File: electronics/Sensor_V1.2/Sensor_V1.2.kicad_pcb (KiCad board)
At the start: 2 copper layers, 45.9 x 25.6 mm, 44 parts, among them J1 nuclone_small_left, J2 nuclone_small_right, J5 DevBoardUartInput, Q1 DMG1012, Q2 DMG1012, Q3 DMG1012, U1 PPG_sensor, U2 reference_sot23-3, U3 MCP6541

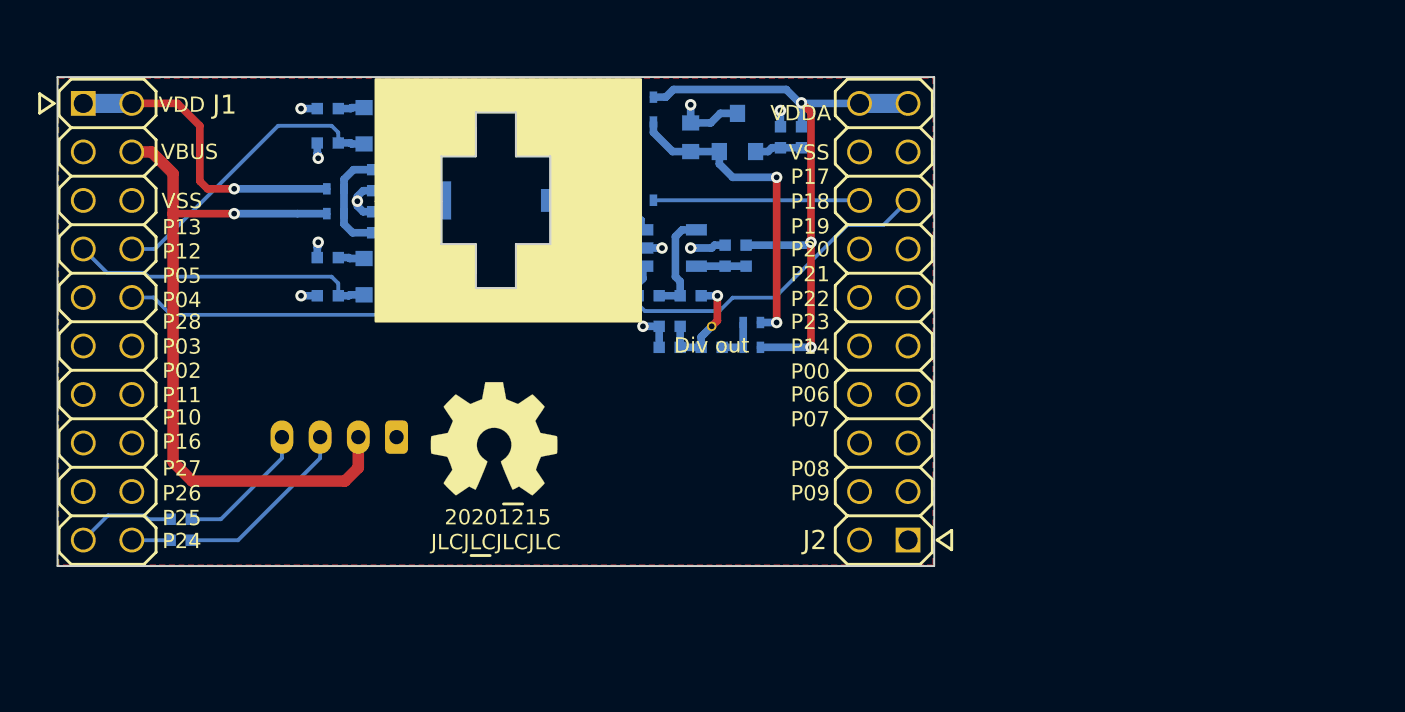
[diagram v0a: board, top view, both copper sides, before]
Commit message: imported some changed components, but need to redo the footprints from TODO
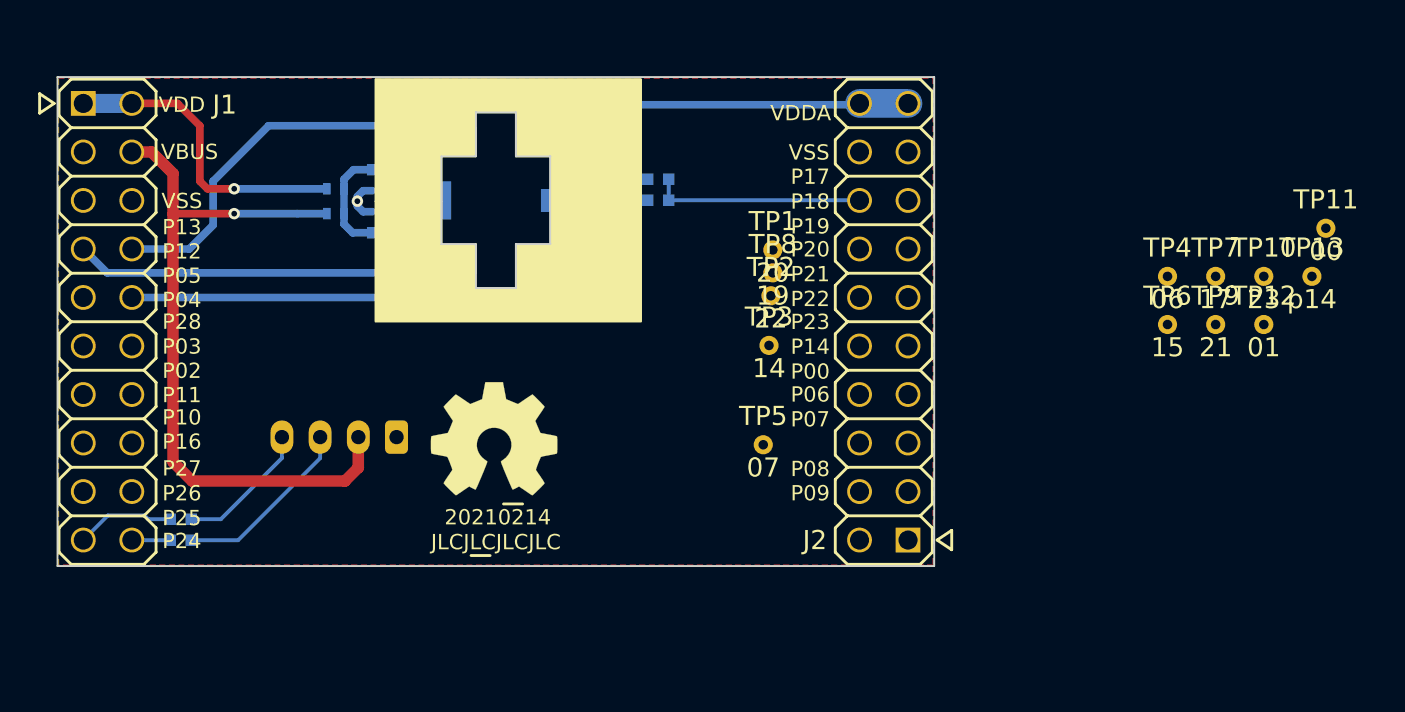
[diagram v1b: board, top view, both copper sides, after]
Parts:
- removed C10, C11, C5: 1u, SquantorRcl:C_0402
- removed C3: 100n, SquantorRcl:C_0402
- removed C6: 10u, SquantorRcl:C_0603
- removed FB1, FB2: Ferrite_Bead, SquantorRcl:L_0402
- removed JP1: bias VDD, SquantorSpecial:solder_jumper_2way_noconn
- removed JP3: bias REF, SquantorSpecial:solder_jumper_2way_noconn
- removed JP4: AVDD divider, SquantorSpecial:solder_jumper_2way_noconn
- removed JP5: VREF divider, SquantorSpecial:solder_jumper_2way_noconn
- removed JP7: PD_ADC, SquantorSpecial:solder_jumper_2way_noconn
- removed Q2, Q3: DMG1012, SquantorIC:SOT23-3
- removed R12, R17, R18, R7: R, SquantorRcl:R_0402_hand
- removed R5, R6: 10K, SquantorRcl:R_0402_hand
- removed U2: reference_sot23-3, SquantorIC:SOT23-3
- removed U3: MCP6541, SquantorIC:SOT23-5-Microchip-OT
- added TP1: 20, SquantorTestPoints:TestPoint_hole_H05R10, F.Cu at (99.6, 82.6)
- added TP10: 23, SquantorTestPoints:TestPoint_hole_H05R10, F.Cu at (125.3, 84.0)
- added TP12: 01, SquantorTestPoints:TestPoint_hole_H05R10, F.Cu at (125.3, 86.5)
- added TP13: p14, SquantorTestPoints:TestPoint_hole_H05R10, F.Cu at (127.8, 84.0)
- added TP2: 22, SquantorTestPoints:TestPoint_hole_H05R10, F.Cu at (99.5, 85.0)
- added TP3: 14, SquantorTestPoints:TestPoint_hole_H05R10, F.Cu at (99.4, 87.6)
- added TP4: 06, SquantorTestPoints:TestPoint_hole_H05R10, F.Cu at (120.3, 84.0)
- added TP5: 07, SquantorTestPoints:TestPoint_hole_H05R10, F.Cu at (99.1, 92.8)
- added TP6: 15, SquantorTestPoints:TestPoint_hole_H05R10, F.Cu at (120.3, 86.5)
- added TP7: 17, SquantorTestPoints:TestPoint_hole_H05R10, F.Cu at (122.8, 84.0)
- added TP8: 19, SquantorTestPoints:TestPoint_hole_H05R10, F.Cu at (99.6, 83.8)
- added TP9: 21, SquantorTestPoints:TestPoint_hole_H05R10, F.Cu at (122.8, 86.5)
- C2: value 100n -> TBD
- N2: value 20201215 -> 20210214
- R3, R4: value 100 -> TBD
- TP11: value Div out -> 00; footprint SquantorTestPoints:TestPoint_hole_H03R05 -> SquantorTestPoints:TestPoint_hole_H05R10
- moved TP11 32.6 mm to (128.6, 81.5)
- moved R4 18.0 mm to (93.6, 80.0)
- moved R3 15.7 mm to (91.6, 79.4), turned to 90 degrees
- moved C2 14.5 mm to (93.6, 78.9), turned to 0 degrees
- moved C1 1.40 mm to (90.2, 76.1)
- moved FB3 0.80 mm to (90.2, 75.0)
- moved R8 0.30 mm to (89.7, 85.0)
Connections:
- C2 pad 1: /LED1_A -> /VSS
- C2 pad 2: /VSS -> /PD_ADC
- FB3 pad 1: Net-(FB3-Pad1) -> /VDDA
- J1 pad 7: /LED1_EN -> /LED1_C
- J1 pad 8: /LED2_EN -> /LED2_C
- J2 pad 1: Net-(J2-Pad1) -> /GPIO_14
- J2 pad 10: Net-(J2-Pad10) -> /P0_14
- J2 pad 11: Net-(J2-Pad11) -> /P0_21
- J2 pad 12: Net-(J2-Pad12) -> /P0_22
- J2 pad 13: Net-(J2-Pad13) -> /P0_19
- J2 pad 14: Net-(J2-Pad14) -> /P0_20
- J2 pad 15: /CMP_OUT -> /P0_17
- J2 pad 2: Net-(J2-Pad2) -> /P0_15
- J2 pad 3: Net-(J2-Pad3) -> /P0_01
- J2 pad 6: Net-(J2-Pad6) -> /P0_07
- J2 pad 7: Net-(J2-Pad7) -> /P0_00
- J2 pad 8: Net-(J2-Pad8) -> /P0_06
- J2 pad 9: Net-(J2-Pad9) -> /P0_23
- R3 pad 1: Net-(Q2-Pad2) -> /PD_OUT
- R4 pad 1: Net-(Q3-Pad2) -> /PD_ADC
- R4 pad 2: /VSS -> /PD_OUT
- TP11 pad 1: /Divider_out -> /P0_00
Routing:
- net /CMP_OUT: track 18.8 -> 0.00 mm
- net /VDDA: track 34.4 -> 16.0 mm, vias 3 -> 0
- net /LED2_C: track 9.06 -> 27.2 mm
- net /LED1_C: track 9.06 -> 26.4 mm
- net /VREF: track 16.8 -> 0.00 mm, vias 2 -> 0
- net /LED1_EN: track 16.1 -> 0.00 mm
- net /LED2_EN: track 15.5 -> 0.00 mm
- net /VSS: track 20.3 -> 9.31 mm, vias 13 -> 5
- net /Divider_out: track 6.10 -> 0.00 mm, vias 1 -> 0
- net Net-(R17-Pad2): track 5.55 -> 0.00 mm
- net Net-(FB3-Pad1): track 3.04 -> 0.00 mm
- net Net-(C10-Pad1): track 2.60 -> 0.00 mm
- net Net-(C5-Pad1): track 2.48 -> 0.00 mm
- net Net-(JP4-Pad2): track 2.40 -> 0.00 mm
- net /PD_BIAS: track 15.9 -> 14.0 mm, vias 2 -> 1
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
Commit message: initial placement of components
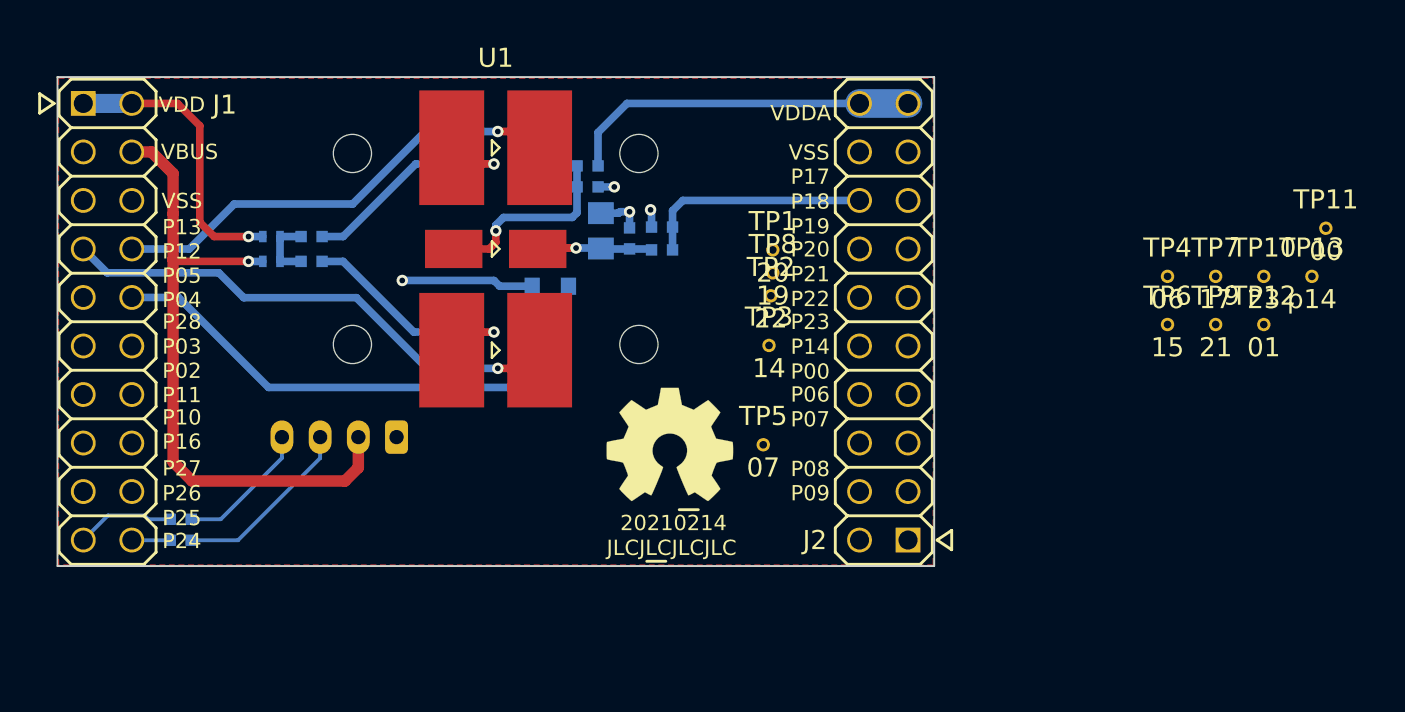
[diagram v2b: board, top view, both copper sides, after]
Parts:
- TP1, TP10, TP11, TP12, TP13, TP2, TP3, TP4, TP5, TP6, TP7, TP8, TP9: footprint SquantorTestPoints:TestPoint_hole_H05R10 -> SquantorTestPoints:TestPoint_hole_H04R07
- U1: footprint SquantorOpto:PPG_sensor_reverse_PD_antiparallel -> SquantorOpto:PPG_sensor_front_universal
- moved N1 9.20 mm to (94.2, 92.8)
- moved N2 9.20 mm to (95.2, 96.8)
- moved N3 9.20 mm to (93.5, 98.3)
- moved R11 5.13 mm to (75.5, 81.9)
- moved JP2 4.18 mm to (73.3, 81.9)
- moved JP6 4.18 mm to (73.3, 83.2)
- moved R10 4.04 mm to (75.5, 83.2)
- moved C1 3.21 mm to (89.9, 79.3)
- moved FB3 3.21 mm to (89.9, 78.2)
- moved C9 2.65 mm to (90.6, 81.6)
- moved R3 2.65 mm to (92.1, 82.0)
- moved R4 2.61 mm to (93.8, 82.6)
- moved U1 2.54 mm to (85.1, 82.5)
- moved C2 2.51 mm to (93.8, 81.4)
- moved R8 2.33 mm to (87.5, 85.9)
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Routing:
- net /LED1_A: track 5.24 -> 13.1 mm, vias 0 -> 1
- net /LED2_A: track 5.28 -> 13.1 mm, vias 0 -> 1
- net /PD_BIAS: track 14.0 -> 10.2 mm
- net /VBUS: track 37.8 -> 34.5 mm
- net /VSS: track 9.31 -> 12.5 mm, vias 5 -> 4
- net /LED2_C: track 27.2 -> 24.2 mm, vias 0 -> 1
- net /VDDA: track 16.0 -> 18.6 mm
- net /LED_VDD: track 5.74 -> 3.50 mm
- net /VDD: track 16.3 -> 15.2 mm
- net /PD_ADC: track 11.1 -> 12.1 mm
- net /I_reset: track 28.4 -> 29.3 mm
- net /PD_OUT: track 6.46 -> 7.37 mm, vias 0 -> 1
- net /LED1_C: track 26.4 -> 26.9 mm, vias 0 -> 1
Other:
- outline, holes or cut-outs redrawn

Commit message: components placed, changing silk
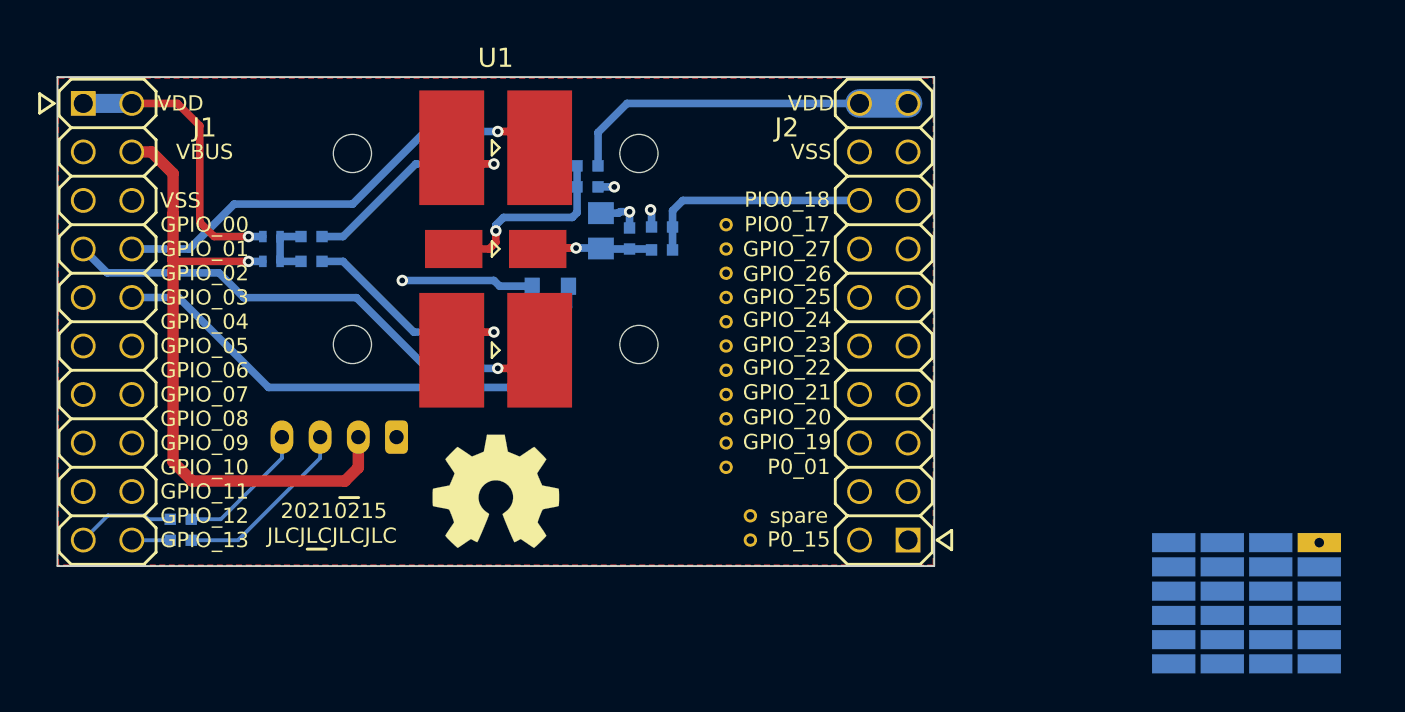
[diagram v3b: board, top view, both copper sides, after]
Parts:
- added J3: Proto_1pin, SquantorProto:proto-SMD-0127-08X06-P010X020+pin, B.Cu at (124.4, 101.1)
- J1: footprint SquantorConnectors:Header-0254-2X10-H010 -> SquantorConnectorsNamed:nuclone_small_left
- J2: footprint SquantorConnectors:Header-0254-2X10-H010 -> SquantorConnectorsNamed:nuclone_small_right
- N2: value 20210214 -> 20210215
- TP1, TP10, TP11, TP12, TP13, TP2, TP3, TP4, TP5, TP6, TP7, TP8, TP9: moved to B.Cu
- moved TP11 32.9 mm to (97.2, 91.4)
- moved TP13 32.0 mm to (98.4, 96.5)
- moved TP12 29.1 mm to (97.2, 94.0)
- moved TP10 28.6 mm to (97.2, 88.9)
- moved TP7 25.8 mm to (97.2, 81.3)
- moved TP9 25.6 mm to (97.2, 86.4)
- moved TP6 24.6 mm to (98.4, 97.8)
- moved TP4 23.9 mm to (97.2, 90.2)
- moved N2 17.8 mm to (77.4, 96.2)
- moved N3 17.8 mm to (75.7, 97.7)
- moved N1 9.43 mm to (85.1, 95.2)
- moved TP1 2.45 mm to (97.2, 82.5)
- moved TP8 2.45 mm to (97.2, 83.8)
- moved TP2 2.35 mm to (97.2, 85.1)
- moved TP3 2.25 mm to (97.2, 87.6)
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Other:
- board text removed: "P00"
- board text removed: "P02"
- board text removed: "P03"
- board text removed: "P04"
- board text removed: "P05"
- board text removed: "P06"
- board text removed: "P07"
- board text removed: "P08"
- board text removed: "P09"
- board text removed: "P10"
- board text removed: "P11"
- board text removed: "P12"
- board text removed: "P13"
- board text removed: "P14"
- board text removed: "P16"
- board text removed: "P17"
- board text removed: "P18"
- board text removed: "P19"
- board text removed: "P20"
- board text removed: "P21"
- board text removed: "P22"
- board text removed: "P23"
- board text removed: "P24"
- board text removed: "P25"
- board text removed: "P26"
- board text removed: "P27"
- board text removed: "P28"
- board text removed: "VBUS"
- board text removed: "VDD"
- board text removed: "VDDA"
- board text removed: "VSS"

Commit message: changed header labels, changed test point labels
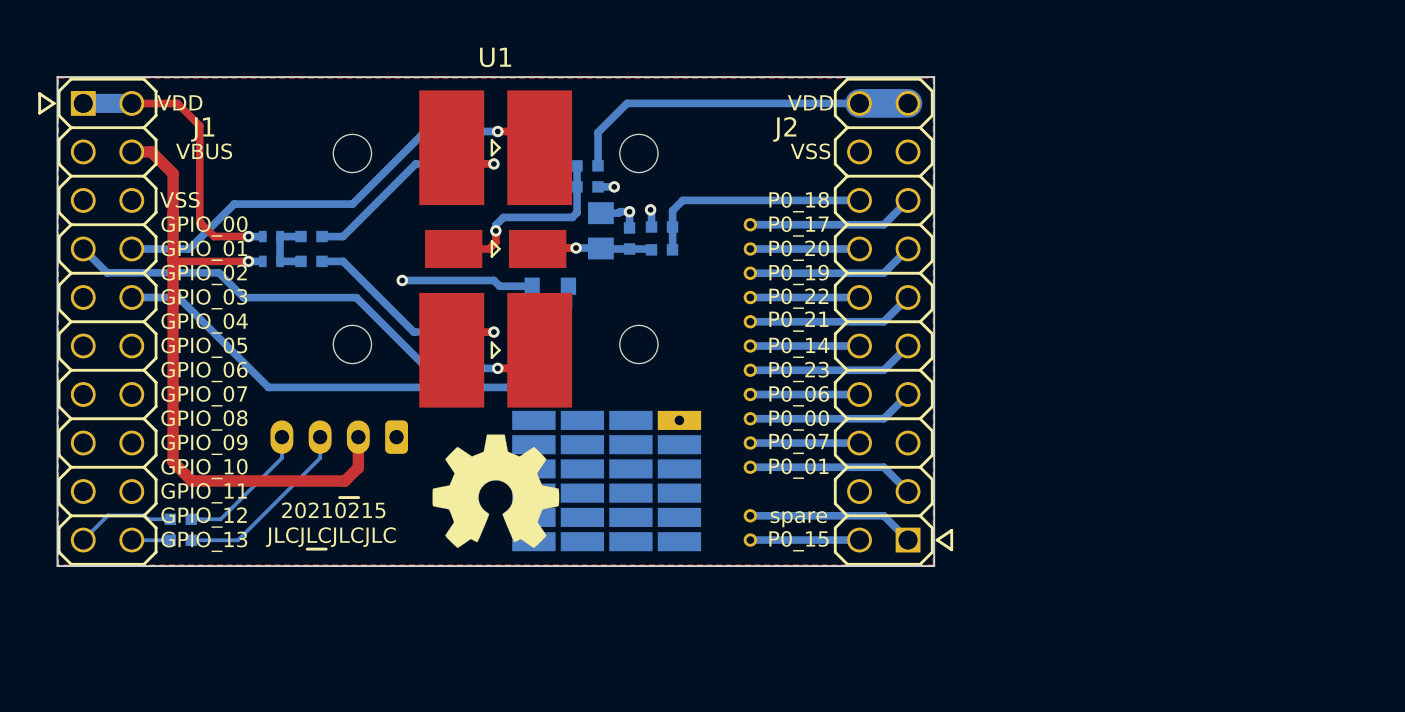
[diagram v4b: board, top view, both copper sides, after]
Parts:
- moved J3 34.1 mm to (90.9, 94.7)
- moved TP1 1.27 mm to (98.4, 82.5)
- moved TP10 1.27 mm to (98.4, 88.9)
- moved TP11 1.27 mm to (98.4, 91.4)
- moved TP12 1.27 mm to (98.4, 94.0)
- moved TP2 1.27 mm to (98.4, 85.1)
- moved TP3 1.27 mm to (98.4, 87.6)
- moved TP4 1.27 mm to (98.4, 90.2)
- moved TP5 1.27 mm to (98.4, 92.7)
- moved TP7 1.27 mm to (98.4, 81.3)
- moved TP8 1.27 mm to (98.4, 83.8)
- moved TP9 1.27 mm to (98.4, 86.4)
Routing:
- net /P0_23: track 0.00 -> 8.78 mm
- net /GPIO_14: track 0.00 -> 8.78 mm
- net /P0_21: track 0.00 -> 8.78 mm
- net /P0_19: track 0.00 -> 8.78 mm
- net /P0_17: track 0.00 -> 8.78 mm
- net /P0_01: track 0.00 -> 8.78 mm
- net /P0_00: track 0.00 -> 8.78 mm
- net /P0_22: track 0.00 -> 5.72 mm
- net /P0_20: track 0.00 -> 5.72 mm
- net /P0_15: track 0.00 -> 5.72 mm
- net /P0_14: track 0.00 -> 5.72 mm
- net /P0_07: track 0.00 -> 5.72 mm
- net /P0_06: track 0.00 -> 5.72 mm
